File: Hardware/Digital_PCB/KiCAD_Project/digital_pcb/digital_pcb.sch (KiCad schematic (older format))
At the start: 35 parts, among them J1 Conn_01x02, J2 ISP, J3 Conn_01x02, J4 Board to Board, J5 Spare 1, U1 STM32F103CBTx, Y1 8MHz

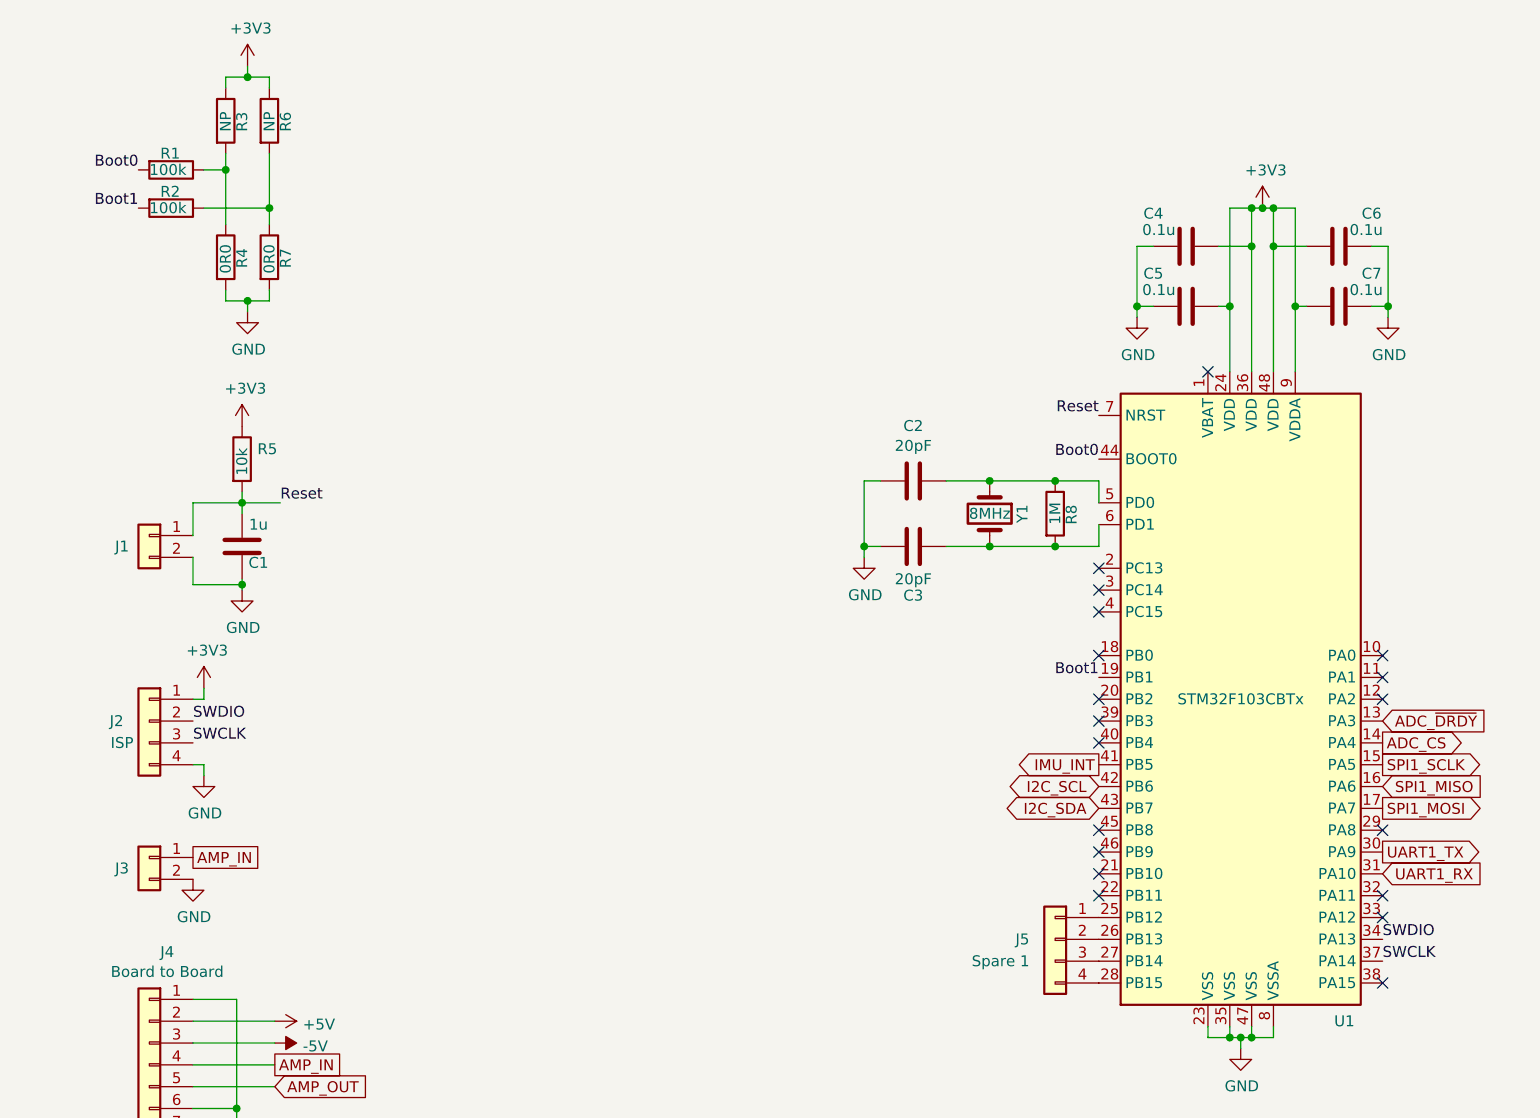
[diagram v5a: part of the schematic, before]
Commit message: Update footprints
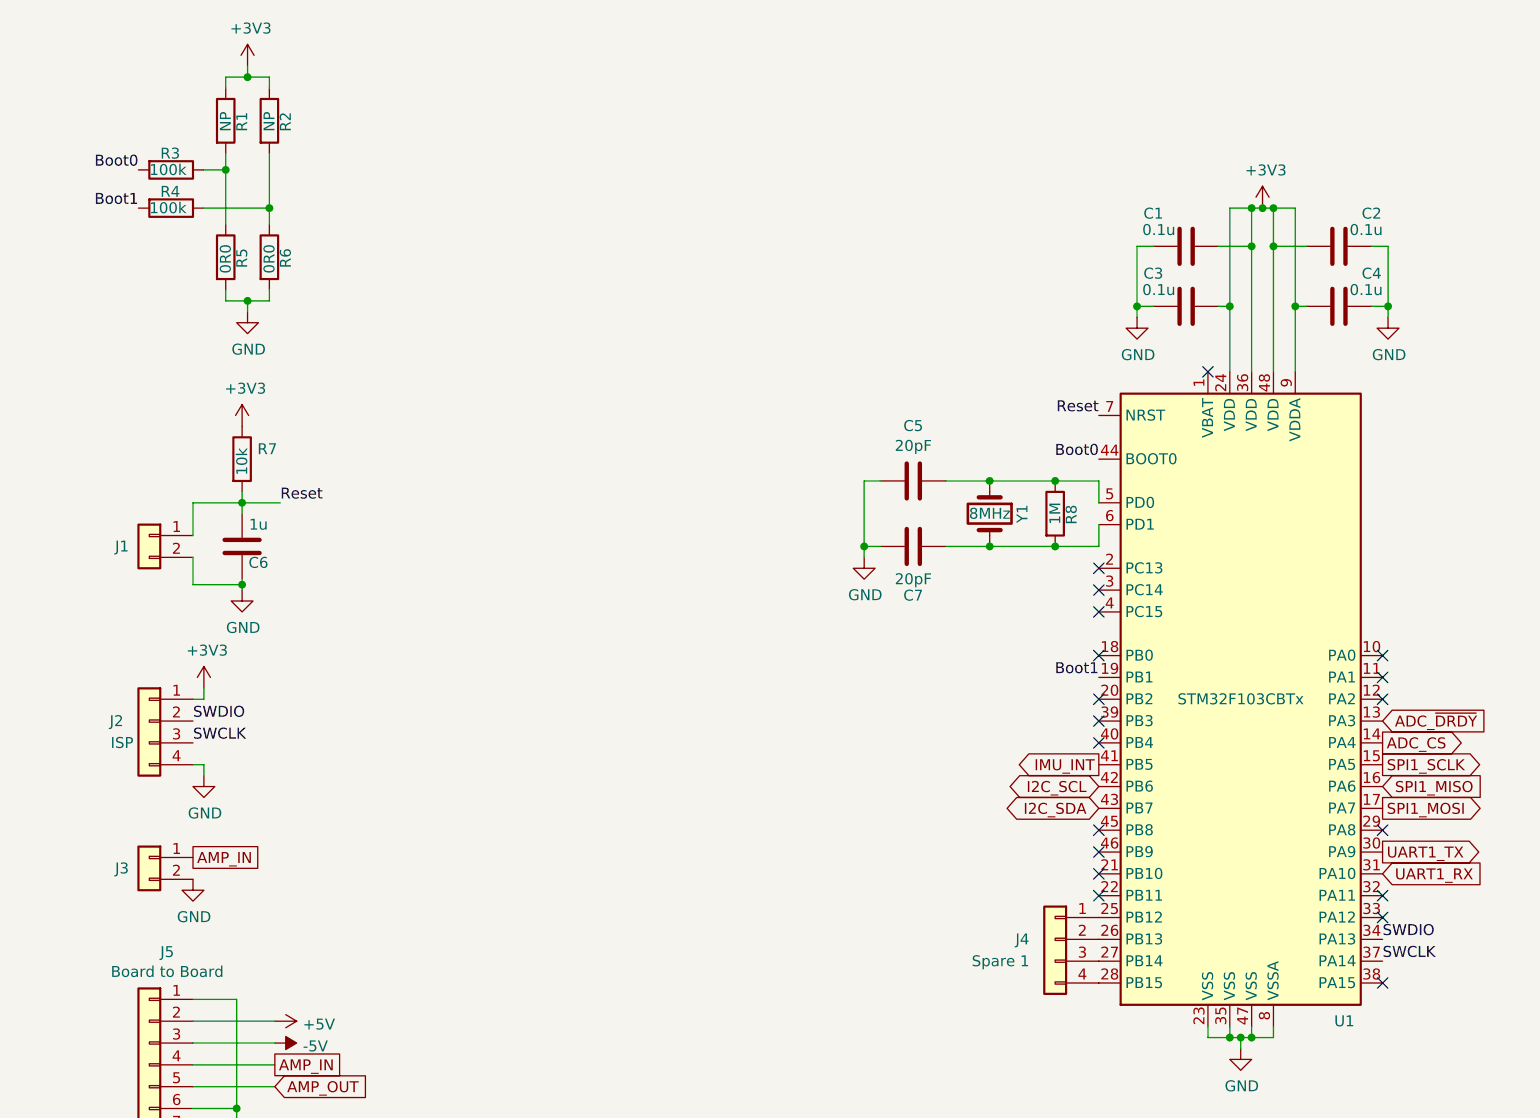
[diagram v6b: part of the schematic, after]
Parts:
- C1: renamed from C4; footprint Capacitors_SMD:C_0603_HandSoldering -> Capacitor_SMD:C_0603_1608Metric
- C2: renamed from C6; footprint Capacitors_SMD:C_0603_HandSoldering -> Capacitor_SMD:C_0603_1608Metric
- C3: renamed from C5; footprint Capacitors_SMD:C_0603_HandSoldering -> Capacitor_SMD:C_0603_1608Metric
- C4: renamed from C7; footprint Capacitors_SMD:C_0603_HandSoldering -> Capacitor_SMD:C_0603_1608Metric
- C5: renamed from C2; footprint Capacitors_SMD:C_0603_HandSoldering -> Capacitor_SMD:C_0603_1608Metric
- C6: renamed from C1; footprint Capacitors_SMD:C_0603_HandSoldering -> Capacitor_SMD:C_0603_1608Metric
- C7: renamed from C3; footprint Capacitors_SMD:C_0603_HandSoldering -> Capacitor_SMD:C_0603_1608Metric
- J1, J3: footprint Pin_Headers:Pin_Header_Straight_1x02_Pitch2.54mm -> Connector_PinHeader_2.54mm:PinHeader_1x02_P2.54mm_Vertical
- J2: footprint Pin_Headers:Pin_Header_Straight_1x04_Pitch2.54mm -> Connector_PinHeader_2.54mm:PinHeader_1x04_P2.54mm_Vertical
- J4: renamed from J5; footprint Pin_Headers:Pin_Header_Straight_1x04_Pitch2.54mm -> Connector_PinHeader_2.54mm:PinHeader_1x04_P2.54mm_Vertical
- J5: renamed from J4; footprint Pin_Headers:Pin_Header_Straight_1x10_Pitch2.54mm -> Connector_PinHeader_2.54mm:PinHeader_1x10_P2.54mm_Vertical
- R1: renamed from R3; footprint Resistors_SMD:R_0603_HandSoldering -> Resistor_SMD:R_0603_1608Metric
- R10, R11, R12, R13, R14, R15, R8, R9: footprint Resistors_SMD:R_0603_HandSoldering -> Resistor_SMD:R_0603_1608Metric
- R2: renamed from R6; footprint Resistors_SMD:R_0603_HandSoldering -> Resistor_SMD:R_0603_1608Metric
- R3: renamed from R1; footprint Resistors_SMD:R_0603_HandSoldering -> Resistor_SMD:R_0603_1608Metric
- R4: renamed from R2; footprint Resistors_SMD:R_0603_HandSoldering -> Resistor_SMD:R_0603_1608Metric
- R5: renamed from R4; footprint Resistors_SMD:R_0603_HandSoldering -> Resistor_SMD:R_0603_1608Metric
- R6: renamed from R7; footprint Resistors_SMD:R_0603_HandSoldering -> Resistor_SMD:R_0603_1608Metric
- R7: renamed from R5; footprint Resistors_SMD:R_0603_HandSoldering -> Resistor_SMD:R_0603_1608Metric

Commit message: Update for Rev 3.0
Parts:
- added PCB1: barepcb, lib_fp:barepcb, symbol lib_sch:barepcb
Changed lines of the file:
@@
 Sheet 1 5
 Title "Digital Rotating Electronics - NSSL EFM"
-Date "2020-12-17"
-Rev "2.0"
+Date "2020-12-18"
+Rev "3.0"
 Comp "Leeman Geophysical LLC"
 Comment1 "(479) 373-3736"
@@
 Wire Wire Line
 	10875 6325 10875 5675
+$Comp
+L lib_sch:barepcb PCB1
+U 1 1 5FE2D163
+P 7225 6400
+F 0 "PCB1" H 7453 6446 50  0000 L CNN
+F 1 "barepcb" H 7075 6425 50  0000 L CNN
+F 2 "lib_fp:barepcb" H 7225 6400 50  0001 C CNN
+F 3 "" H 7225 6400 50  0001 C CNN
+F 4 "3-0000069" H 7225 6400 50  0001 C CNN "Internal Part Number"
+F 5 "1" H 7225 6400 50  0001 C CNN "Populated"
+	1    7225 6400
+	1    0    0    -1
+$EndComp
 $EndSCHEMATC

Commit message: Change PN for header to plug into analog PCBA.
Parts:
- J5: Internal Part Number 1-0000557 -> 1-0000455
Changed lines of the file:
@@
 F 2 "Connector_PinHeader_2.54mm:PinHeader_1x10_P2.54mm_Vertical" H 1025 5650 50  0001 C CNN
 F 3 "~" H 1025 5650 50  0001 C CNN
-F 4 "1-0000557" H 1025 5650 50  0001 C CNN "Internal Part Number"
+F 4 "1-0000455" H 1025 5650 50  0001 C CNN "Internal Part Number"
 F 5 "1" H 1025 5650 50  0001 C CNN "Populated"
 	1    1025 5650
